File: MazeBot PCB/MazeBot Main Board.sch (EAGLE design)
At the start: 44 parts, among them IC1 7805TV, IC2 L298, Q1 16MHz

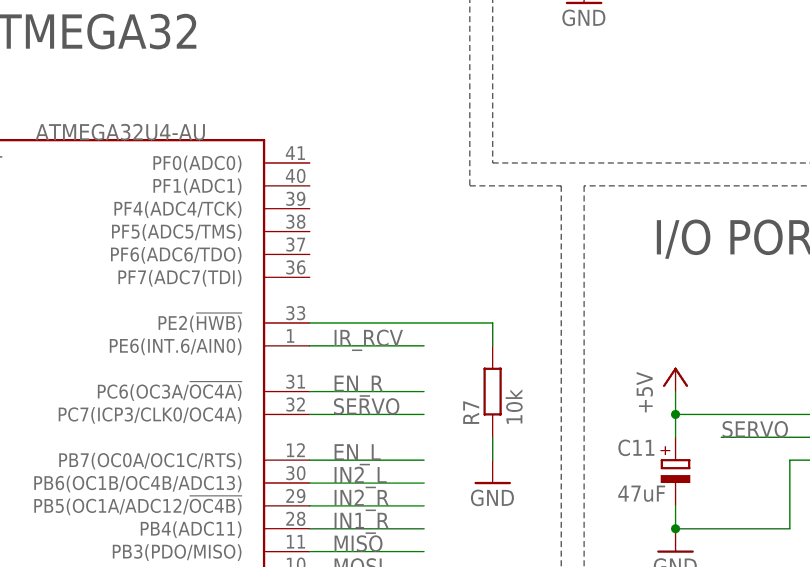
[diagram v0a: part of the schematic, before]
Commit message: Add jumper to HWB
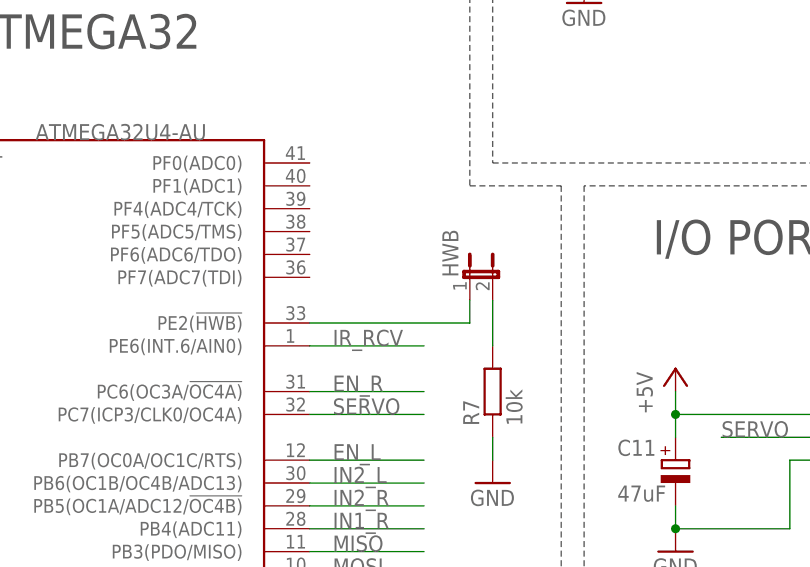
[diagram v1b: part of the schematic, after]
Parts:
- added HWB: (no value), jumper:JP1E
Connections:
- new net N$9: HWB.2, R7.2
- net N$8: now also HWB.1; no longer R7.2
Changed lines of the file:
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@@
 <part name="R7" library="eagle-ltspice" library_urn="urn:adsk.eagle:library:217" deviceset="R" device="R1206" package3d_urn="urn:adsk.eagle:package:13301/1" value="10k"/>
 <part name="GND24" library="supply1" library_urn="urn:adsk.eagle:library:371" deviceset="GND" device=""/>
+<part name="HWB" library="jumper" library_urn="urn:adsk.eagle:library:252" deviceset="JP1E" device="" package3d_urn="urn:adsk.eagle:package:15455/1"/>
 </parts>
 <sheets>
@@
 <attribute name="VALUE" x="160.02" y="66.04" size="1.778" layer="96"/>
 </instance>
+<instance part="HWB" gate="A" x="160.02" y="91.44" smashed="yes">
+<attribute name="NAME" x="158.75" y="91.44" size="1.778" layer="95" rot="R90"/>
+<attribute name="VALUE" x="165.735" y="91.44" size="1.778" layer="96" rot="R90"/>
+</instance>
 </instances>
 <busses>
@@
 <segment>
 <pinref part="U$1" gate="G$1" pin="PE2(!HWB)"/>
-<wire x1="142.24" y1="86.36" x2="162.56" y2="86.36" width="0.1524" layer="91"/>
-<wire x1="162.56" y1="86.36" x2="162.56" y2="83.82" width="0.1524" layer="91"/>
+<wire x1="142.24" y1="86.36" x2="160.02" y2="86.36" width="0.1524" layer="91"/>
+<pinref part="HWB" gate="A" pin="1"/>
+<wire x1="160.02" y1="86.36" x2="160.02" y2="88.9" width="0.1524" layer="91"/>
+</segment>
+</net>
+<net name="N$9" class="0">
+<segment>
+<pinref part="HWB" gate="A" pin="2"/>
 <pinref part="R7" gate="G$1" pin="2"/>
-</segment>
-</net>
+<wire x1="162.56" y1="88.9" x2="162.56" y2="83.82" width="0.1524" layer="91"/>
+</segment>
+</net>

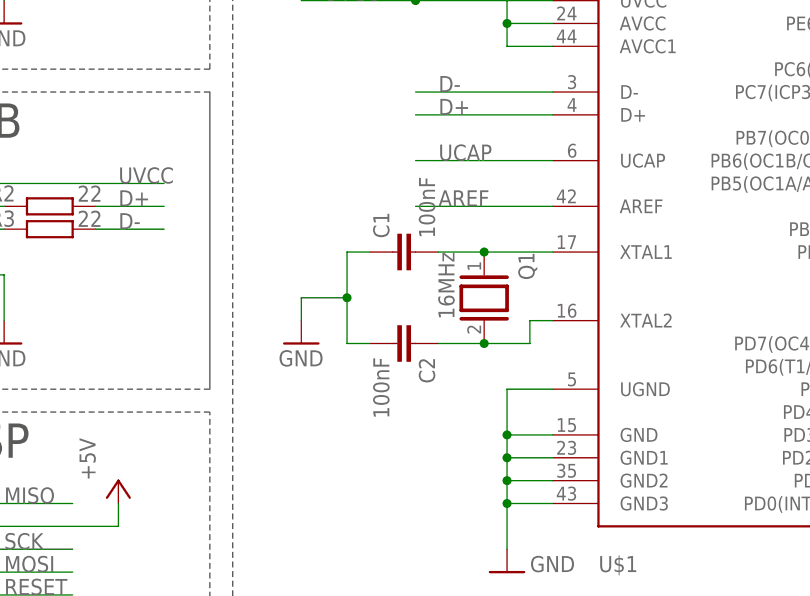
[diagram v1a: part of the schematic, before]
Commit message: Fix XTAL caps
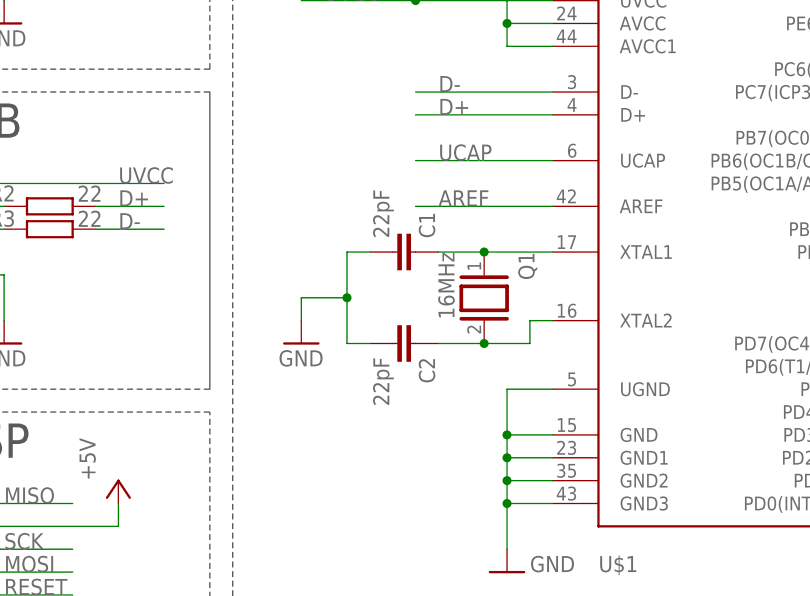
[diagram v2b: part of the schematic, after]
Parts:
- C1, C2: value 100nF -> 22pF
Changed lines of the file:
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@@
 <part name="Q1" library="special" library_urn="urn:adsk.eagle:library:367" deviceset="XTAL/S" device="" package3d_urn="urn:adsk.eagle:package:26647/2" value="16MHz"/>
 <part name="U$1" library="adafruit" deviceset="ATMEGA32U4" device="-AU"/>
-<part name="C1" library="rcl" library_urn="urn:adsk.eagle:library:334" deviceset="C-EU" device="025-024X044" package3d_urn="urn:adsk.eagle:package:23630/1" value="100nF"/>
-<part name="C2" library="rcl" library_urn="urn:adsk.eagle:library:334" deviceset="C-EU" device="025-024X044" package3d_urn="urn:adsk.eagle:package:23630/1" value="100nF"/>
+<part name="C1" library="rcl" library_urn="urn:adsk.eagle:library:334" deviceset="C-EU" device="025-024X044" package3d_urn="urn:adsk.eagle:package:23630/1" value="22pF"/>
+<part name="C2" library="rcl" library_urn="urn:adsk.eagle:library:334" deviceset="C-EU" device="025-024X044" package3d_urn="urn:adsk.eagle:package:23630/1" value="22pF"/>
 <part name="GND9" library="supply1" library_urn="urn:adsk.eagle:library:371" deviceset="GND" device=""/>
 <part name="P+6" library="supply1" library_urn="urn:adsk.eagle:library:371" deviceset="+5V" device=""/>
@@
 </instance>
 <instance part="C1" gate="G$1" x="76.2" y="58.42" smashed="yes" rot="R90">
-<attribute name="NAME" x="75.819" y="59.944" size="1.778" layer="95" rot="R90"/>
-<attribute name="VALUE" x="80.899" y="59.944" size="1.778" layer="96" rot="R90"/>
+<attribute name="NAME" x="80.899" y="59.944" size="1.778" layer="95" rot="R90"/>
+<attribute name="VALUE" x="75.819" y="59.944" size="1.778" layer="96" rot="R90"/>
 </instance>
 <instance part="C2" gate="G$1" x="78.74" y="48.26" smashed="yes" rot="R270">

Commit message: PCB print day upload
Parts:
- added L1: 600Ω/500mA, SparkFun-Coils:INDUCTOR-0805-3.3UH
- C3, C4: value 100nF -> 0.1uF
- C5: value 47uF -> 0.33uF; device rcl:CPOL-EUUD-6,3X8,8 -> rcl:CPOL-EUUD-4X5,8
- C6: value 47uF -> 0.1uF; device rcl:CPOL-EUUD-6,3X8,8 -> rcl:C-EU025-024X044
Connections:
- new net N$10: L1.1, USB.VBUS
- net +5V: now also C6.1, U$1.AVCC, U$1.AVCC1, U$1.VCC, U$1.VCC1; no longer C6.+
- net GND: now also C6.2; no longer C6.-
- net RESET: no longer U$1.AVCC, U$1.AVCC1, U$1.VCC, U$1.VCC1
- net UVCC: now also L1.2; no longer USB.VBUS
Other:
- note added: "POWER SUPPLY"
- note removed: "STABILISER"
- moved on the sheet: C10, C11, C3, C4, C5, D1, D2, D3, D4, D5, D6, D7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

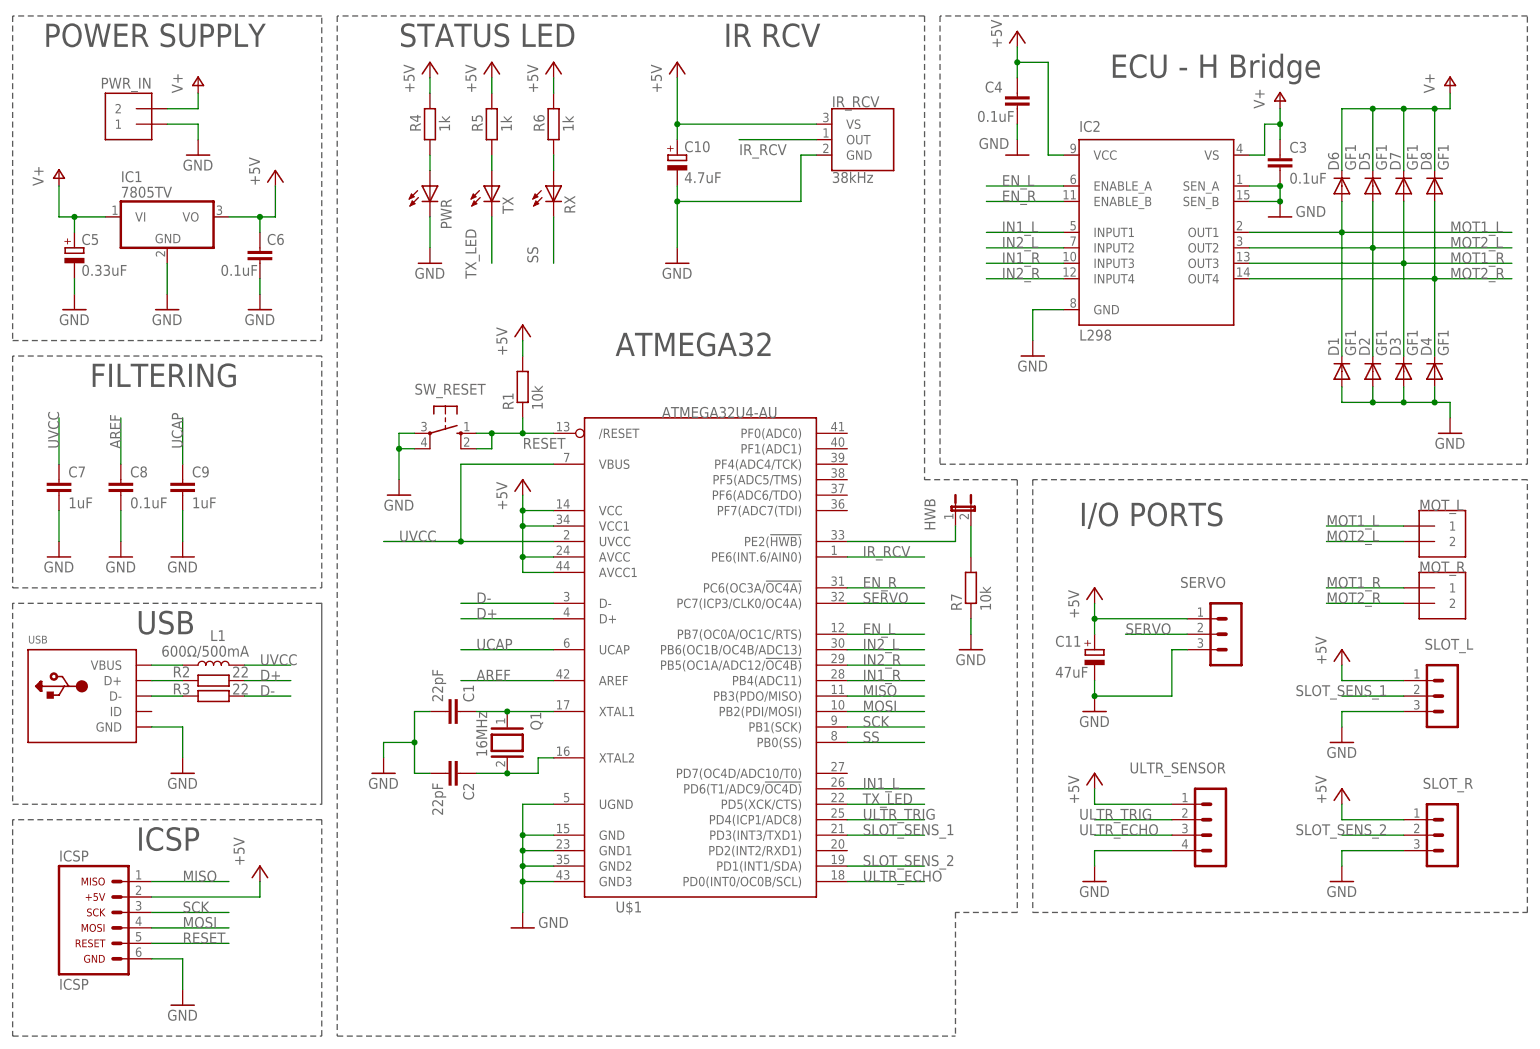
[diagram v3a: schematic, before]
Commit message: Final schamtic cleanup for documentation
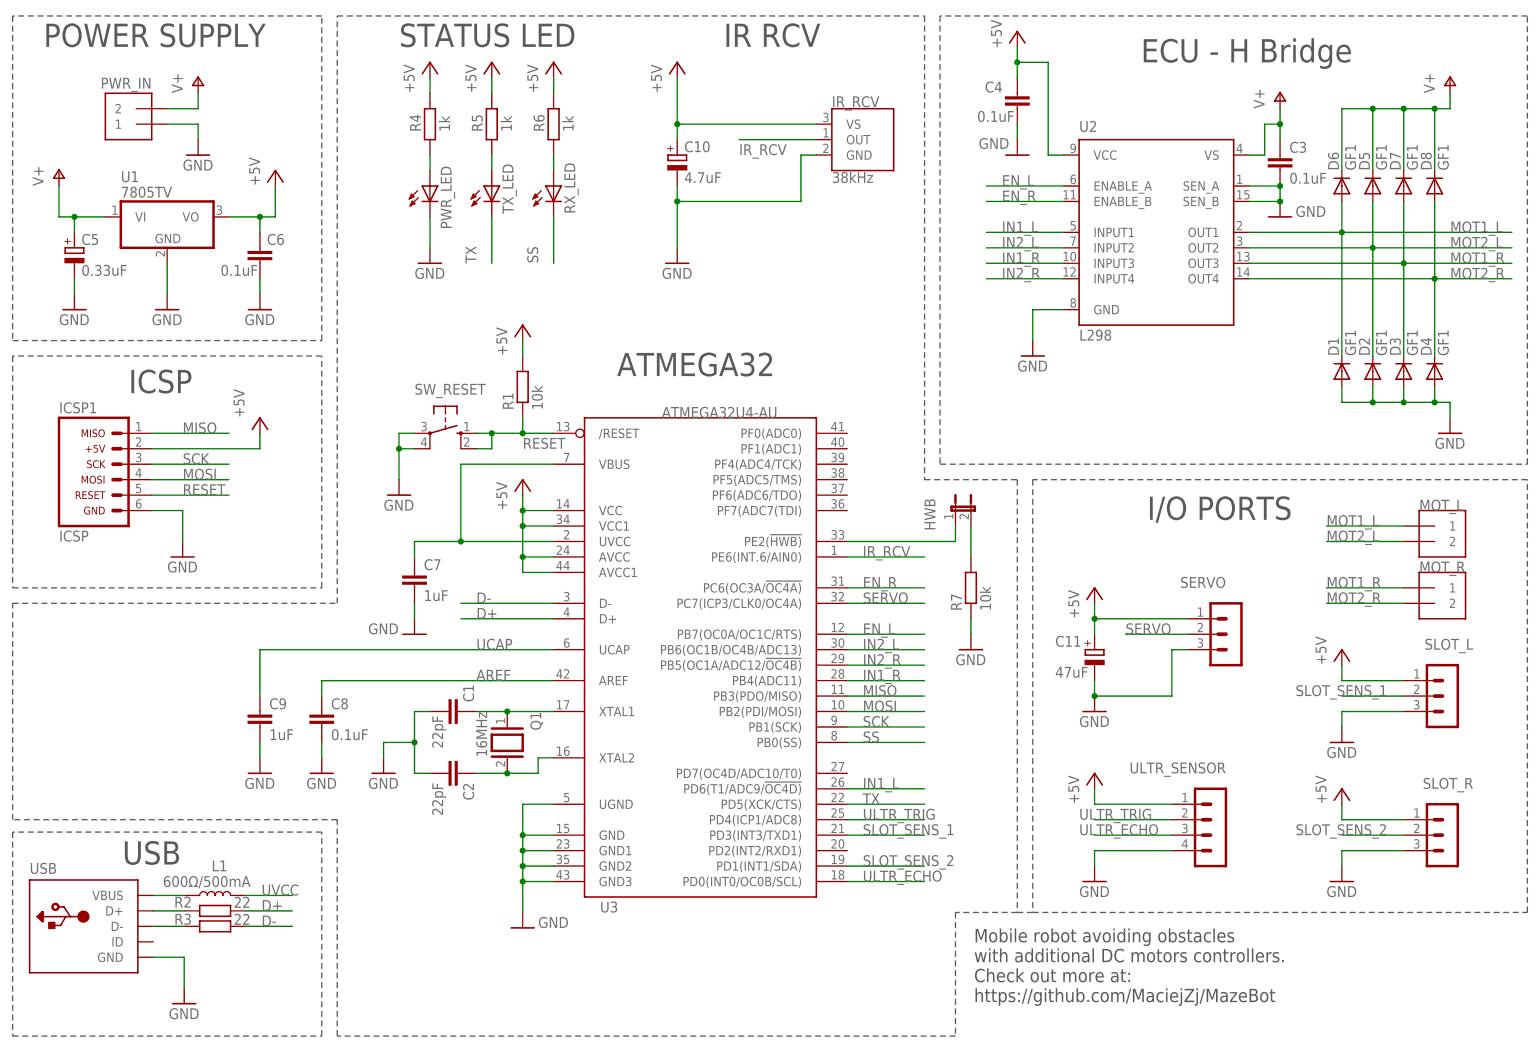
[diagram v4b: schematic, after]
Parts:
- removed ICSP: (no value), arduino_jw:ARDUINO_CONN-ICSP
- added ICSP1: (no value), arduino_jw:ARDUINO_CONN-ICSP
- renumbered IC1 to U1, IC2 to U2, PWR to PWR_LED, RX to RX_LED, TX to TX_LED, U$1 to U3
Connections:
- net TX_LED renamed TX
- net +5V: now also ICSP1.2; no longer ICSP.2
- net GND: now also ICSP1.6; no longer ICSP.6
- net MISO: now also ICSP1.1; no longer ICSP.1
- net MOSI: now also ICSP1.4; no longer ICSP.4
- net RESET: now also ICSP1.5; no longer ICSP.5
- net SCK: now also ICSP1.3; no longer ICSP.3
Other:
- note added: "Mobile robot avoiding obstacles with additional DC motors controllers. Check out more at: https://github.com/MaciejZj/MazeBot"
- note removed: "FILTERING"
- moved on the sheet: C7, C8, C9, L1, R2, R3, USB
